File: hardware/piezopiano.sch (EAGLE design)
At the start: 58 parts, among them J1 CON2, Q1 DMN3404L, Q100 DMP3099L, Q2 DMN3404L, Q3 DMN3404L, Q4 DMN3404L, Q5 DMN3404L, Q6 DMN3404L, Q7 DMN3404L, Q8 DMN3404L, U1 MEGA48A-AU, U100 AP7381-50Y-13

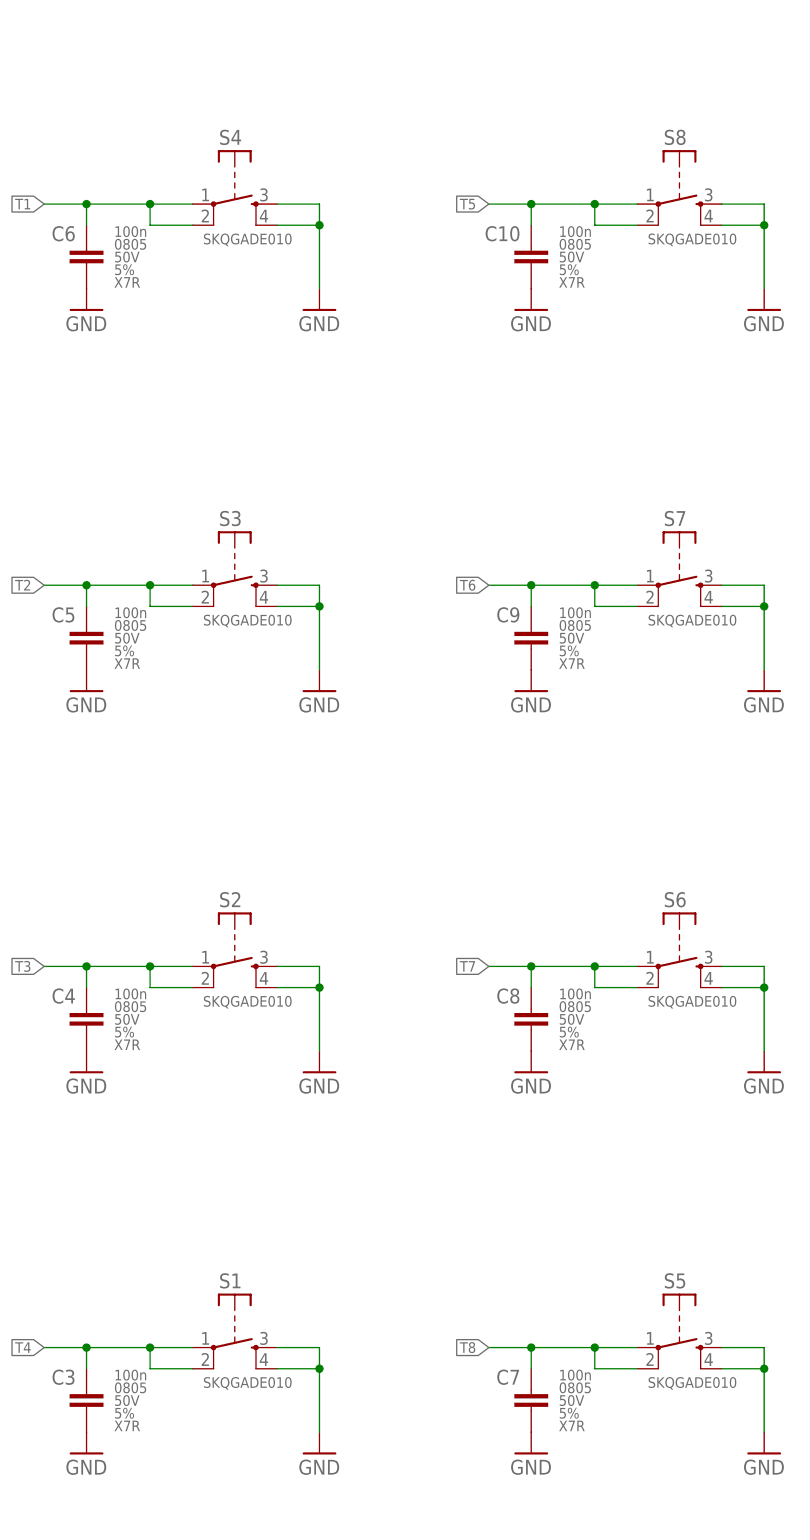
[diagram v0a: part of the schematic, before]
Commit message: Improved 3D piezo model
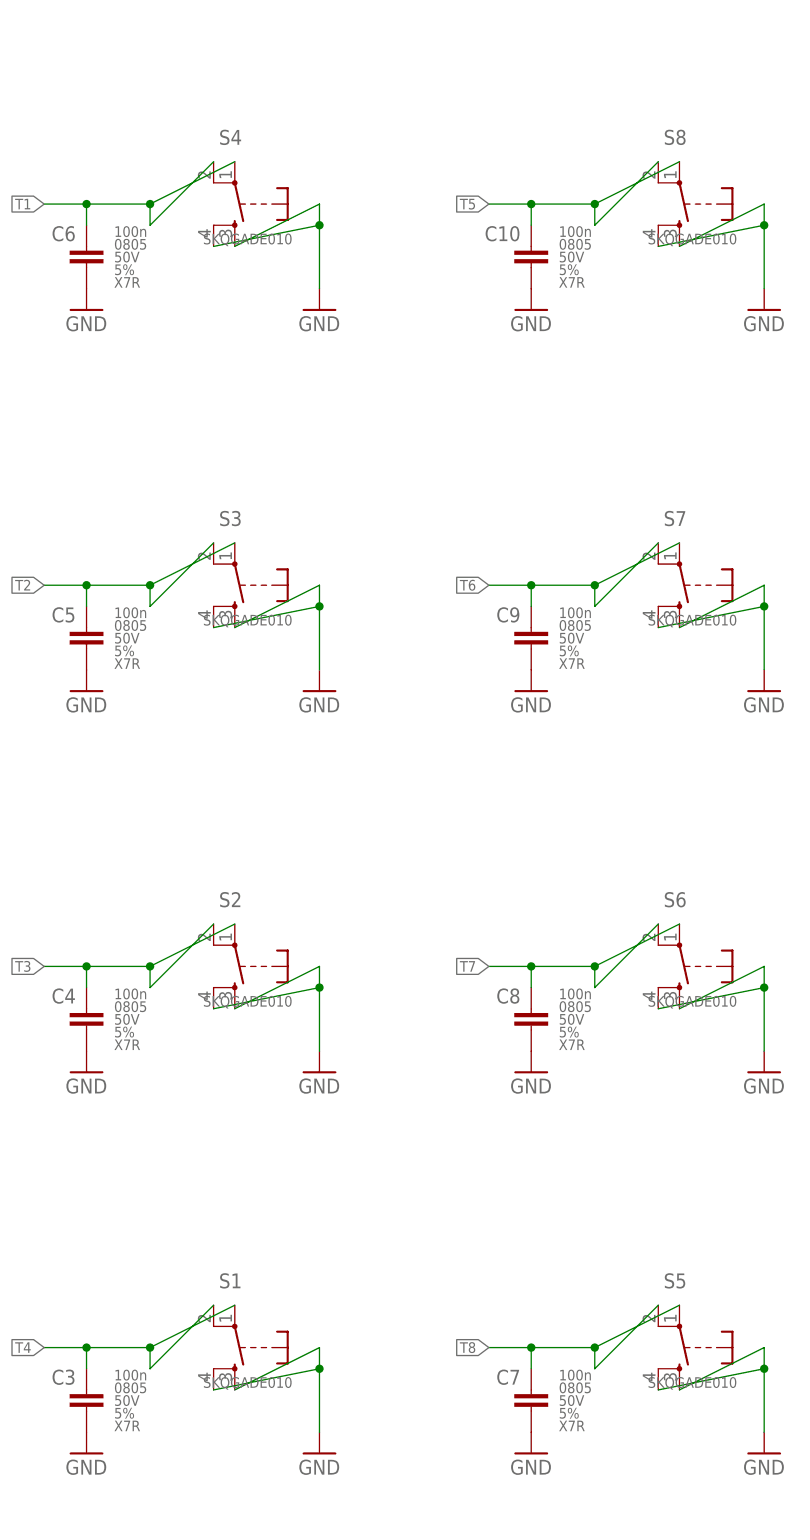
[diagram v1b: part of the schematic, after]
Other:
- moved on the sheet: S1, S2, S3, S4, S5, S6, S7, S8

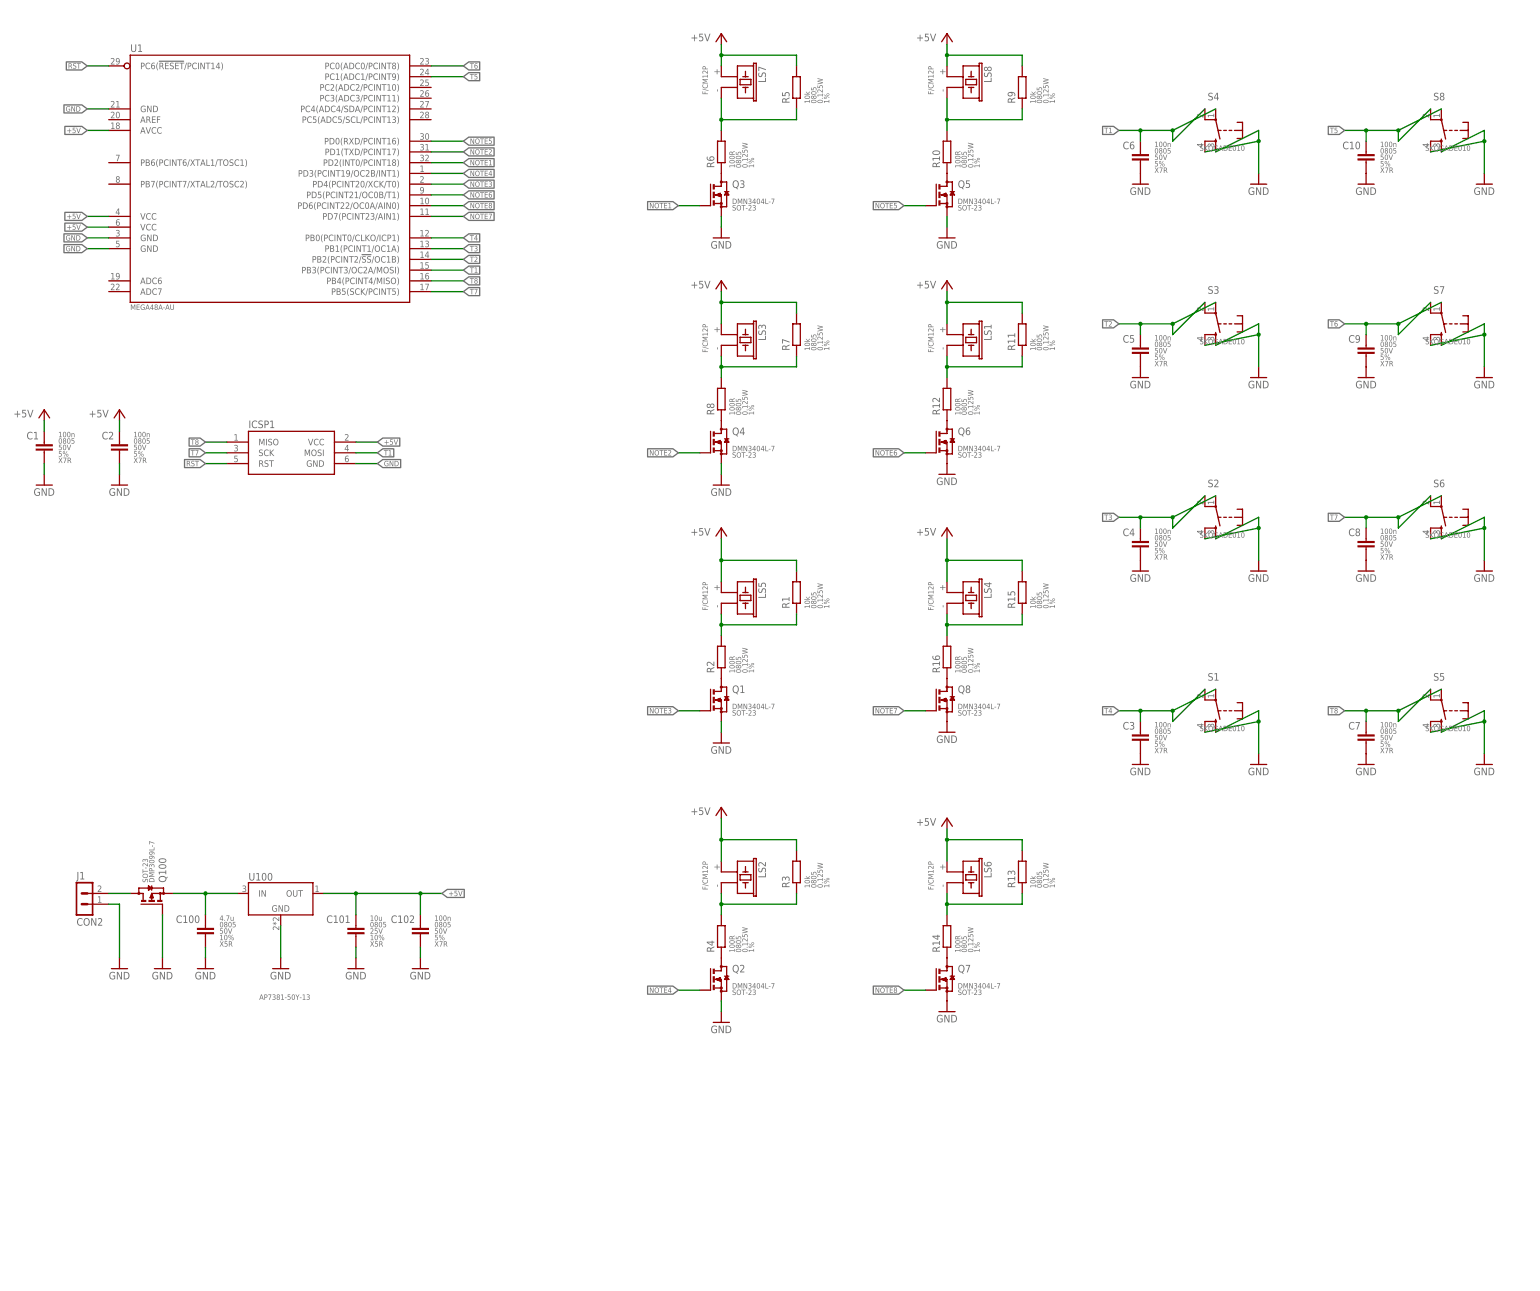
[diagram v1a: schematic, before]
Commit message: Added USB C and UART
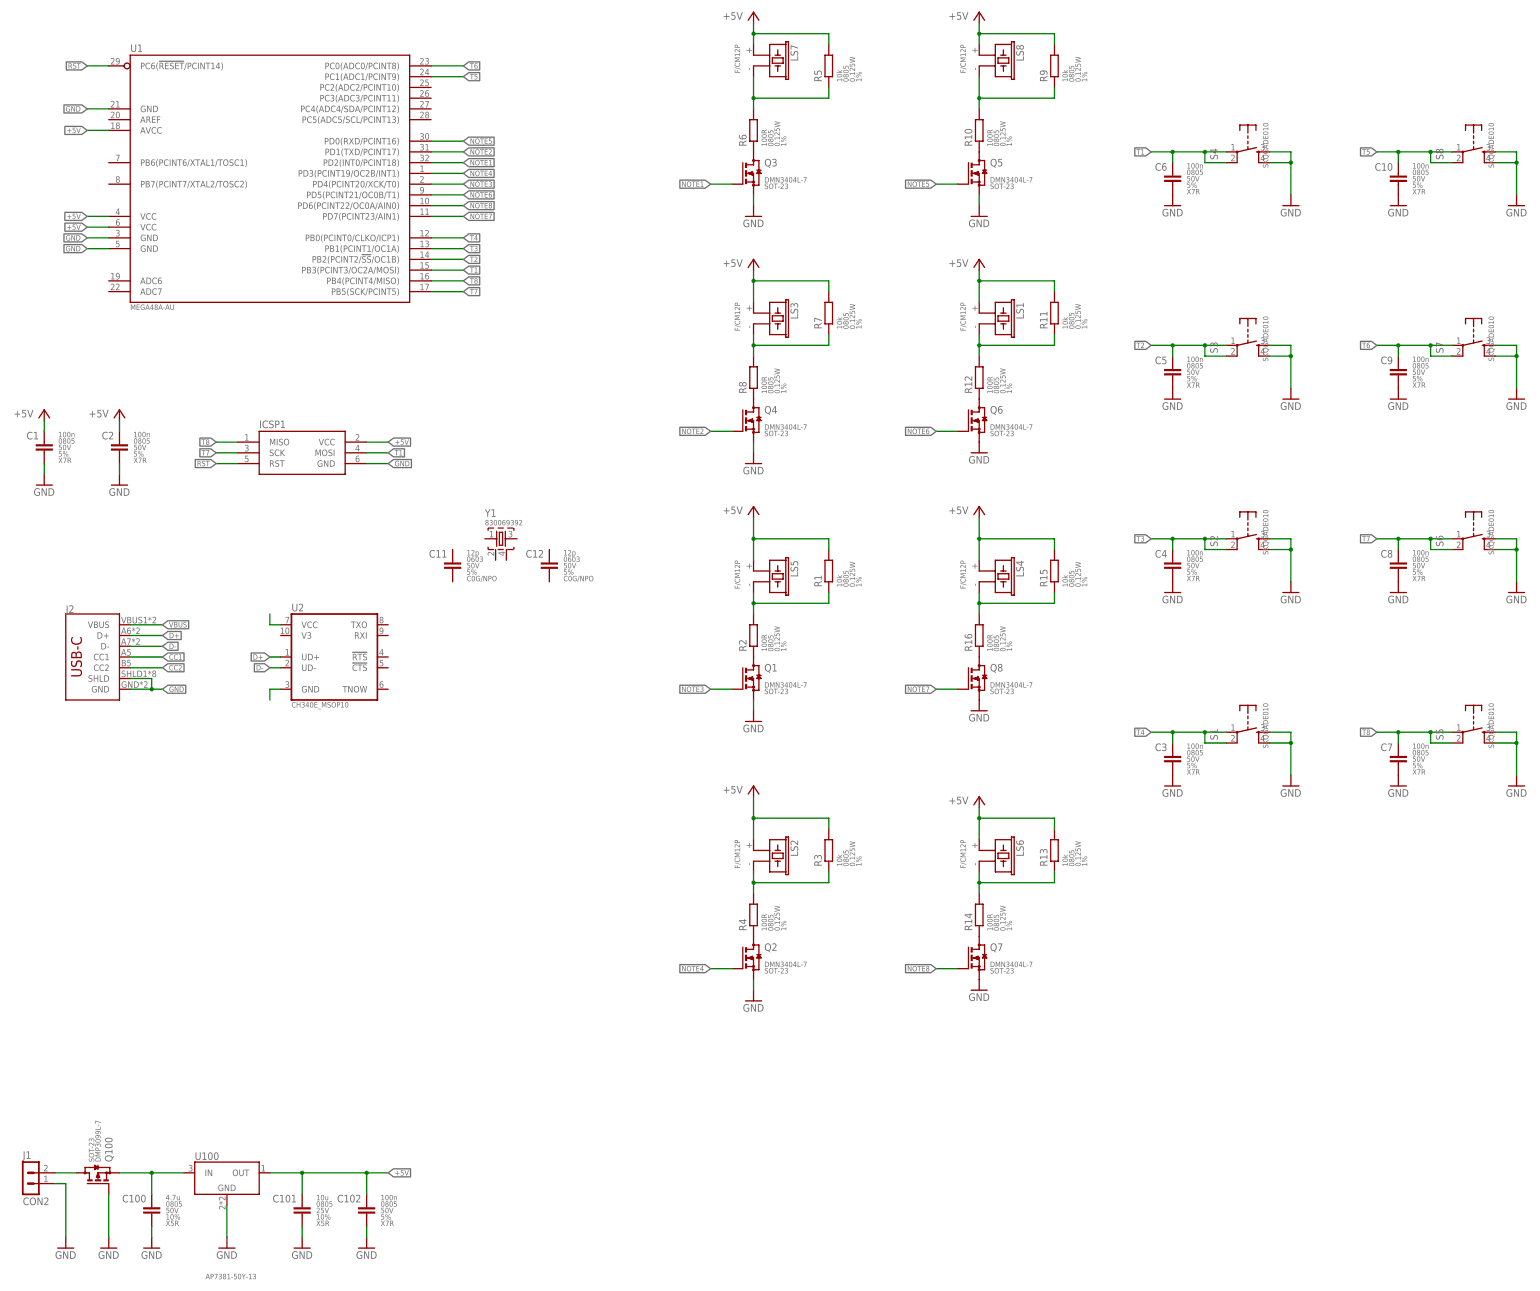
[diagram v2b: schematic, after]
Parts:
- added C11, C12: 12p, zaan-Capacitors:12PF-0603-50V-5%
- added J2: (no value), zaan-Connectors:USB_C2-LAYER
- added U2: CH340E_MSOP10, zaan-IC-General:CH340E_MSOP10
- added Y1: 830069392, zaan-Electromechanical:830069392
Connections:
- new net CC1: J2.CC1
- new net CC2: J2.CC2
- new net D+: J2.D+, U2.UD+
- new net D-: J2.D-, U2.UD-
- new net N$19: U2.VCC
- new net N$20: U2.GND
- new net VBUS: J2.VBUS
- net GND: now also J2.GND, J2.SHLD
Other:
- moved on the sheet: C10, C100, C101, C102, C3, C4, C5, C6, C7, C8, C9, ICSP1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

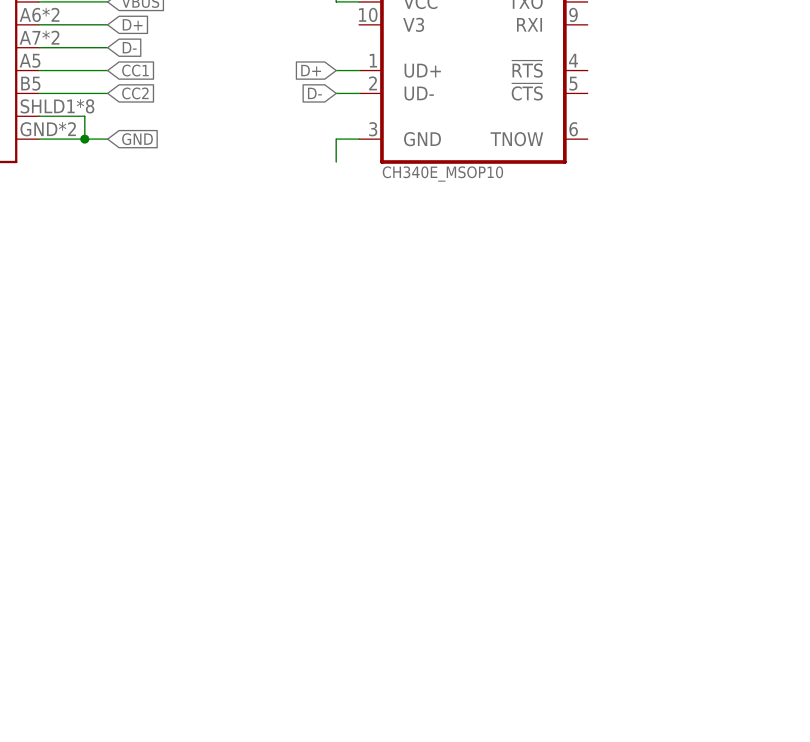
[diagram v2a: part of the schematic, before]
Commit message: Added Battery Connector
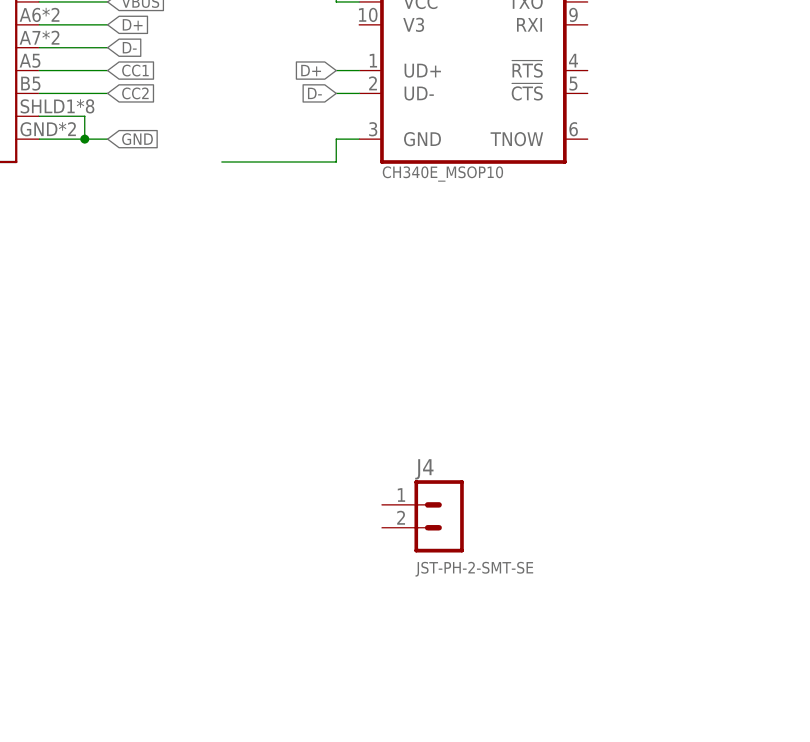
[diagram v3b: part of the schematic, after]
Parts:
- added J4: JST-PH-2-SMT-SE, zaan-Connectors:JST-PH-2-SMT-SE
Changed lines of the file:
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@@
 <part name="C11" library="zaan-Capacitors" library_urn="urn:adsk.eagle:library:16758934" deviceset="12PF" device="-0603-50V-5%" package3d_urn="urn:adsk.eagle:package:16758953/1" value="12p"/>
 <part name="C12" library="zaan-Capacitors" library_urn="urn:adsk.eagle:library:16758934" deviceset="12PF" device="-0603-50V-5%" package3d_urn="urn:adsk.eagle:package:16758953/1" value="12p"/>
+<part name="J4" library="zaan-Connectors" library_urn="urn:adsk.eagle:library:16759010" deviceset="JST-PH-2" device="-SMT-SE" package3d_urn="urn:adsk.eagle:package:16759071/1"/>
 </parts>
 <sheets>
@@
 <attribute name="TOLERANCE" x="140.462" y="116.586" size="1.27" layer="96" align="center-left"/>
 <attribute name="DIELECTRIC" x="140.462" y="115.062" size="1.27" layer="96" align="center-left"/>
+</instance>
+<instance part="J4" gate="G$1" x="81.28" y="45.72" smashed="yes">
+<attribute name="VALUE" x="80.01" y="40.64" size="1.27" layer="96"/>
+<attribute name="NAME" x="80.01" y="51.562" size="1.778" layer="95"/>
 </instance>
 </instances>
@@
 <wire x1="73.66" y1="88.9" x2="71.12" y2="88.9" width="0.1524" layer="91"/>
 <wire x1="71.12" y1="88.9" x2="71.12" y2="86.36" width="0.1524" layer="91"/>
-</segment>
-</net>
+<wire x1="58.42" y1="86.36" x2="71.12" y2="86.36" width="0.1524" layer="91"/>
+</segment>
+</net>

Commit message: Added Battery Management IC
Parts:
- removed Q100: DMP3099L, zaan-Discrete:DMP3099L
- removed U100: AP7381-50Y-13, zaan-IC-Power:AP7381-50Y-13
- added D1, D2: LTST-C171KSKT, zaan-Optoelectronics:LTST-C171KSKT
- added F1: MF-PSMF035X-2, zaan-Fuses:MF-PSMF035X-2
- added R17: 10k, zaan-Resistors:10KOHM-0603-1/10W-1%
- added R18, R19: 5.1k, zaan-Resistors:5.1KOHM-0603-1/10W-1%
- added R20: 0R, zaan-Resistors:0OHM-0603-1/10W-1%
- added S9: TS-1101-C-W, zaan-Electromechanical:TS-1101-C-W
- added U3: TP4333, zaan-IC-Power:TP4333
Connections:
- removed net N$19: U2.VCC
- removed net N$20: U2.GND
- new net N$21: C101.1, J4.2, U3.BAT
- new net N$22: U3.SW
- new net N$23: R17.1, U3.SWT
- new net N$24: R17.2, S9.P
- new net N$25: D1.A, U3.LED1
- new net N$26: D2.A, U3.LED2
- net +5V: now also F1.2, R20.2, U2.VCC, U3.OUT; no longer C101.1, C102.1, U100.OUT
- net GND: now also D1.C, D2.C, J4.1, S9.S, U2.GND, U3.GND; no longer Q100.G, U100.GND
- net N$1: no longer Q100.D
- net N$17: now also R20.1, U3.VDD; no longer Q100.S, U100.IN
- net VBUS: now also F1.1
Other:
- moved on the sheet: C10, C100, C101, C102, C3, C4, C5, C6, C7, C8, C9, J1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
